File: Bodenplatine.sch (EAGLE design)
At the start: 113 parts, among them K1 RY612012, K2 RY612012, K3 RY612012, K4 RY612012, K5 RY612012, K6 RY612012, K7 RY612012, K8 RY612012, K9 RY612012, Q1 BC846BLT1SMD, Q2 BC846BLT1SMD, Q3 BC846BLT1SMD, Q4 BC846BLT1SMD, Q5 BC846BLT1SMD, Q6 BC846BLT1SMD, Q7 BC846BLT1SMD, Q8 BC846BLT1SMD, Q9 BC846BLT1SMD, X1 SPRINGCON_AST125_5X2, X10 SPRINGCON_AST125_3X2, X11 SPRINGCON_AST125_4X2, X12 SPRINGCON_AST125_4X2, X13 SPRINGCON_AST125_5X2, X14 236-403, X15 236-402, X2 SPRINGCON_AST125_5X2, X3 SPRINGCON_AST125_5X2, X4 SPRINGCON_AST125_5X2, X5 SPRINGCON_AST125_5X2, X6 SPRINGCON_AST125_5X2, X7 SPRINGCON_AST125_5X2, X8 SPRINGCON_AST125_5X2, X9 SPRINGCON_AST125_5X2

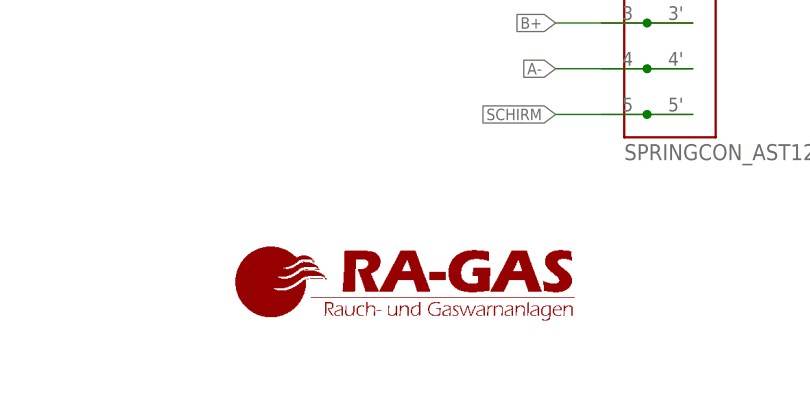
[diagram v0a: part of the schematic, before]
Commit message: A3 Rahmen in BRD eingefügt
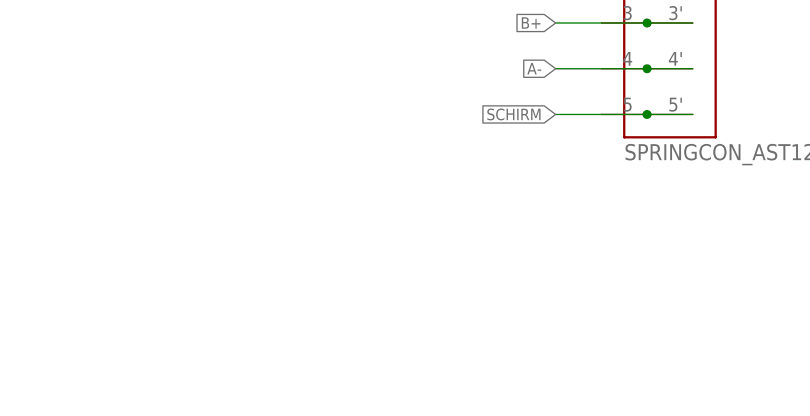
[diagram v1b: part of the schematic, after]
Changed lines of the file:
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@@
 <setting verticaltext="up"/>
 </settings>
-<grid distance="0.1" unitdist="inch" unit="mic" style="lines" multiple="1" display="no" altdistance="0.01" altunitdist="inch" altunit="inch"/>
+<grid distance="0.1" unitdist="inch" unit="inch" style="lines" multiple="1" display="no" altdistance="0.01" altunitdist="inch" altunit="inch"/>
 <layers>
 <layer number="1" name="Top" color="4" fill="1" visible="no" active="no"/>
@@
 <attribute name="OC_FARNELL" value="2317836"/>
 </part>
-<part name="U$6" library="xMZ-Mod-Touch-Bodenplatine" deviceset="LOGO_RA-GAS" device=""/>
 </parts>
 <sheets>
@@
 <attribute name="MPN" x="297.18" y="226.06" size="1.27" layer="96" display="off"/>
 </instance>
-<instance part="U$6" gate="G$1" x="302.26" y="15.24"/>
 </instances>
 <busses>
